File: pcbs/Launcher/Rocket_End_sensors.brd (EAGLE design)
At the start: 100 x 80 mm, 5 parts, among them U1 ARDUINO-MEGAPRO-5V, X1 22-23-2051, X3 22-23-2041

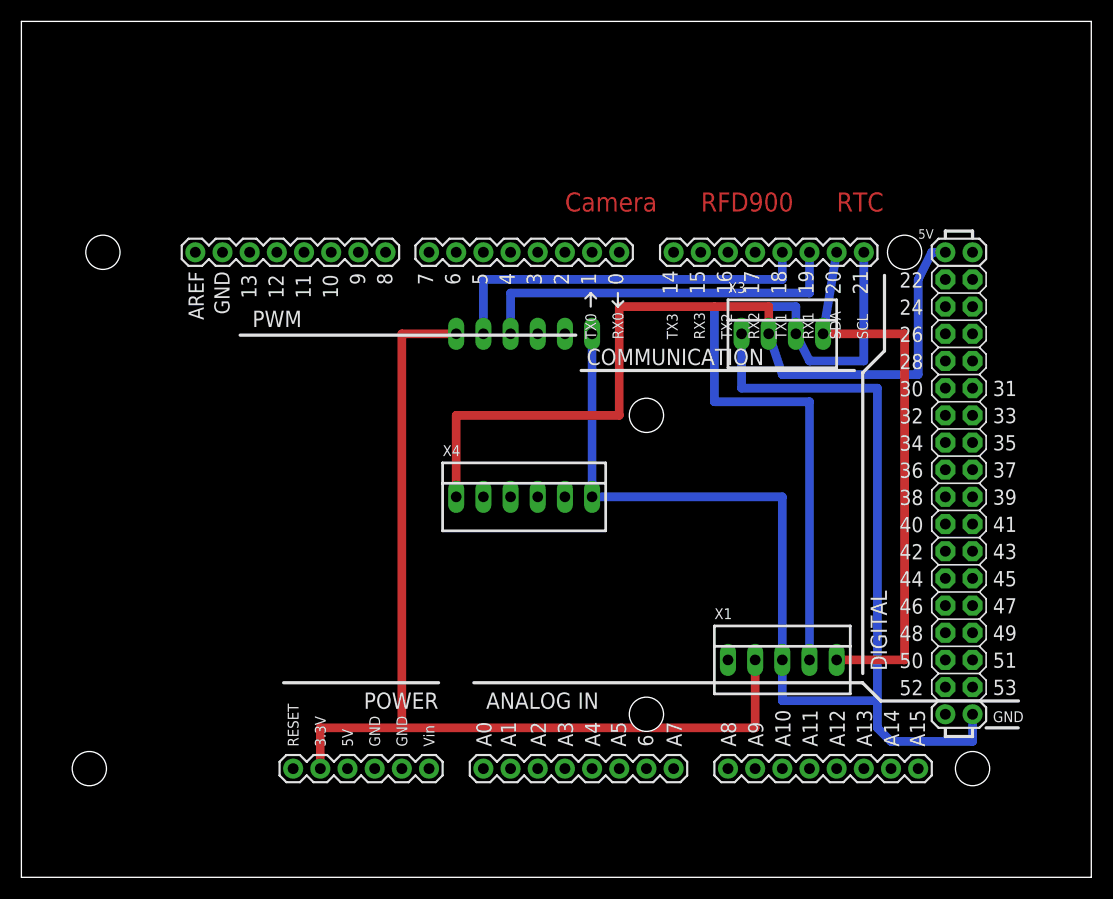
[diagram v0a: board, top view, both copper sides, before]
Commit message: * Adding GPS Module
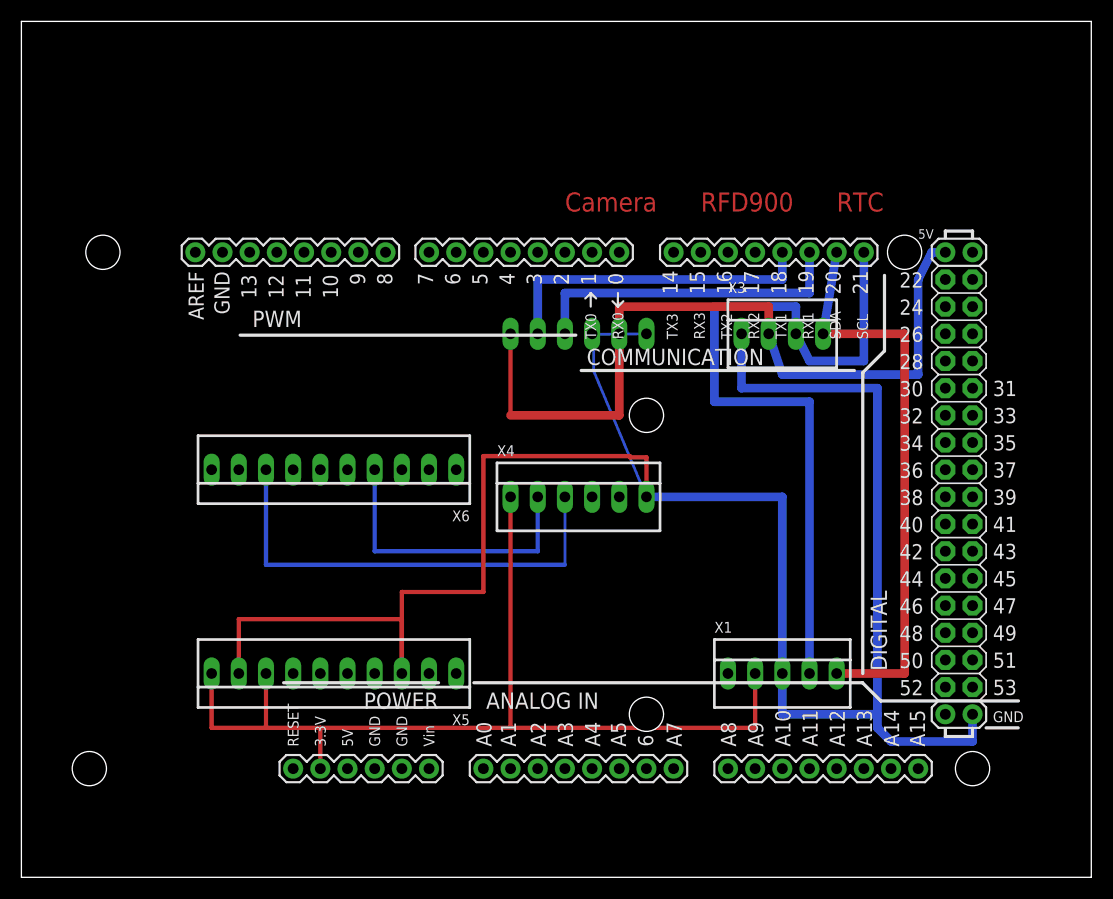
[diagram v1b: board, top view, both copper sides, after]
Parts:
- added X5, X6: 22-23-2101, con-molex:22-23-2101
- moved X2 5.08 mm to (52.1, 50.8)
- moved X4 5.08 mm to (52.1, 35.6)
- moved X1 1.27 mm to (71.1, 19.1)
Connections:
- removed net N$2: U1.3.3V, X1.2, X2.6
- removed net N$5: X4.3
- new net N$4: U1.3.3V, X1.2, X4.1, X5.10, X5.8
- new net N$8: X4.2, X6.4
- net GND: now also X5.3, X5.9
- net N$28: now also X2.6; no longer X4.1
- net N$6: now also X4.3, X6.8; no longer X4.2
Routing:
- net N$2: track 92.7 -> 0.00 mm
- net N$4: track 0.00 -> 91.4 mm
- net GND: track 122.4 -> 196.9 mm
- net N$6: track 0.00 -> 43.2 mm
- net N$8: track 0.00 -> 27.9 mm
- net N$3: track 35.6 -> 30.5 mm
- net N$28: track 79.2 -> 74.2 mm
- net N$1: track 35.6 -> 30.5 mm
- net N$24: track 70.1 -> 71.4 mm
- net N$18: track 52.2 -> 53.4 mm

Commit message: * Much better placement of components and tracks for Rocket_End * Put IMU on bottom of the Sensor board
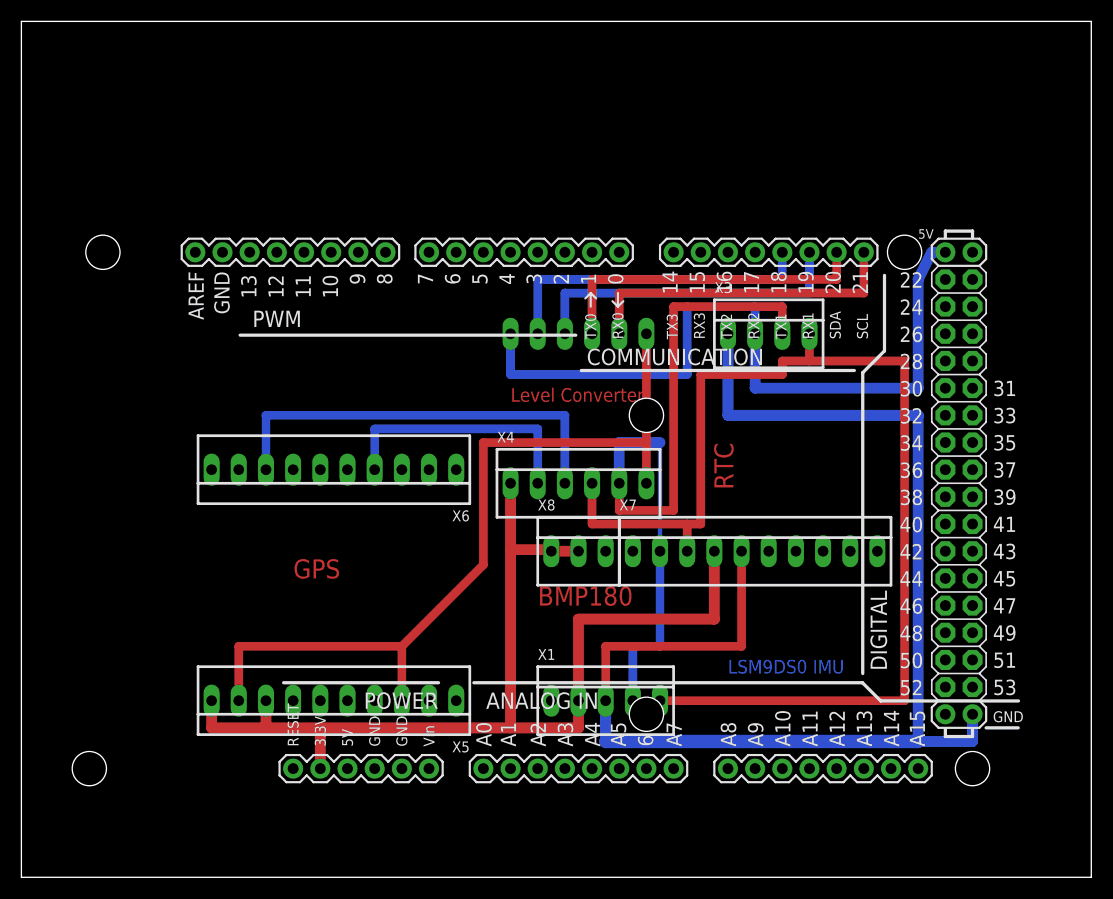
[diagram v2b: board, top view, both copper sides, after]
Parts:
- added X7: 22-23-2101, con-molex:22-23-2101
- added X8: 22-23-2031, con-molex:22-23-2031
- moved X1 16.7 mm to (54.6, 16.5)
- moved X5 2.54 mm to (29.2, 16.5)
- moved X3 1.27 mm to (69.8, 50.8)
- moved X4 1.27 mm to (52.1, 36.8)
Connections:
- new net N$2: U1.21, X2.2
- new net N$5: U1.20, X2.3
- new net N$7: X2.1, X4.6, X5.3, X5.9
- net GND: now also X7.5; no longer X2.1, X4.6, X5.3, X5.9
- net N$18: now also X4.4, X7.3; no longer U1.20
- net N$24: now also X4.5, X7.2; no longer U1.21
- net N$4: now also X7.4, X8.1, X8.2
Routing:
- net N$7: track 0.00 -> 76.8 mm
- net GND: track 196.9 -> 123.2 mm
- net N$18: track 53.4 -> 107.9 mm
- net N$5: track 0.00 -> 30.5 mm
- net N$2: track 0.00 -> 30.5 mm
- net N$4: track 91.4 -> 101.7 mm
- net N$28: track 74.2 -> 70.1 mm
- net N$8: track 27.9 -> 24.1 mm
- net N$6: track 43.2 -> 39.4 mm
- net N$24: track 71.4 -> 73.7 mm
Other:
- board text added: "BMP180"
- board text added: "GPS"
- board text added: "LSM9DS0 IMU"
- board text added: "Level Converter"
- board text removed: "Camera"
- board text removed: "RFD900"

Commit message: * using Via to ensure soldering is done on correct side.
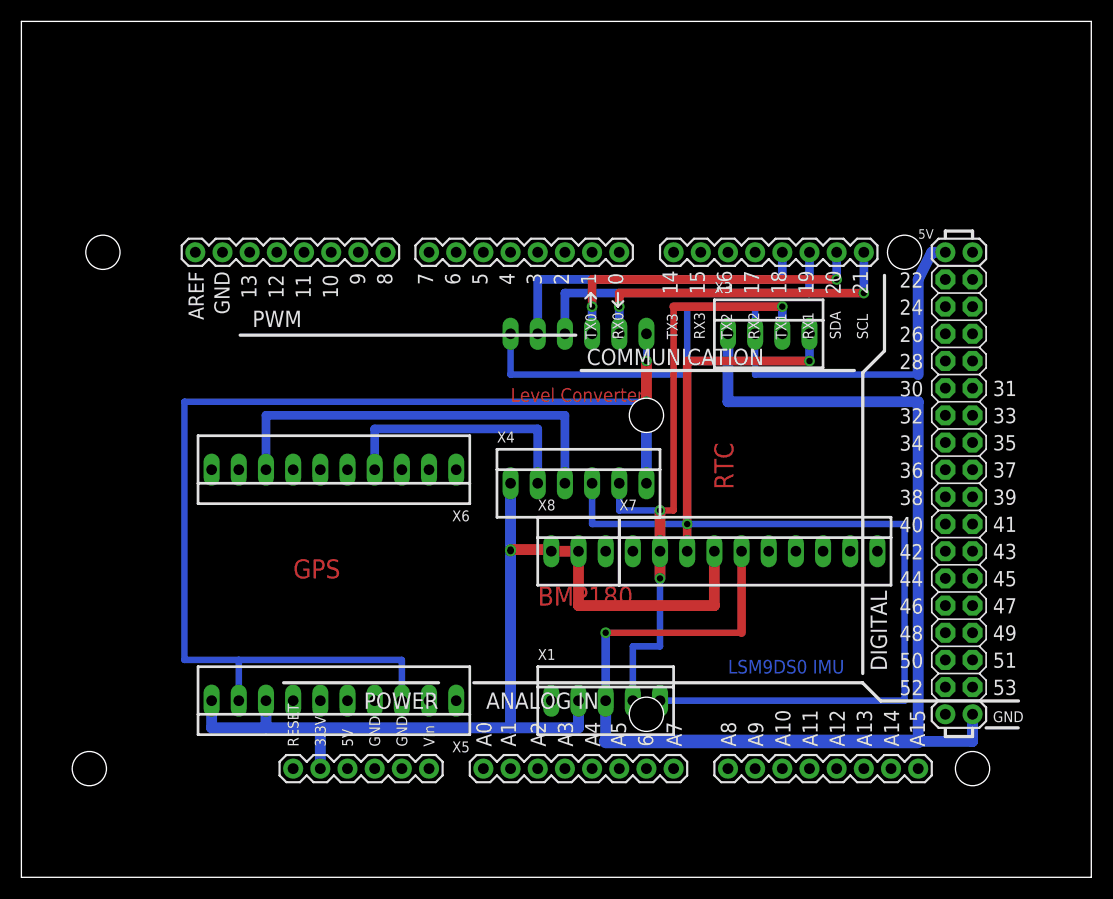
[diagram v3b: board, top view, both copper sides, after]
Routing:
- net N$7: track 76.8 -> 109.2 mm, vias 0 -> 2
- net N$24: track 73.7 -> 59.7 mm, vias 0 -> 3
- net N$4: track 101.7 -> 97.7 mm, vias 0 -> 2
- net N$18: track 107.9 -> 104.1 mm, vias 0 -> 2
- net N$28: track 70.1 -> 67.6 mm
- net N$5: vias 0 -> 2
- net N$2: vias 0 -> 2
- net GND: vias 0 -> 1

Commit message: * More mods....fixed up gps wiring. * Making place where can run some wires underneath so don't need   two sides for relay board.
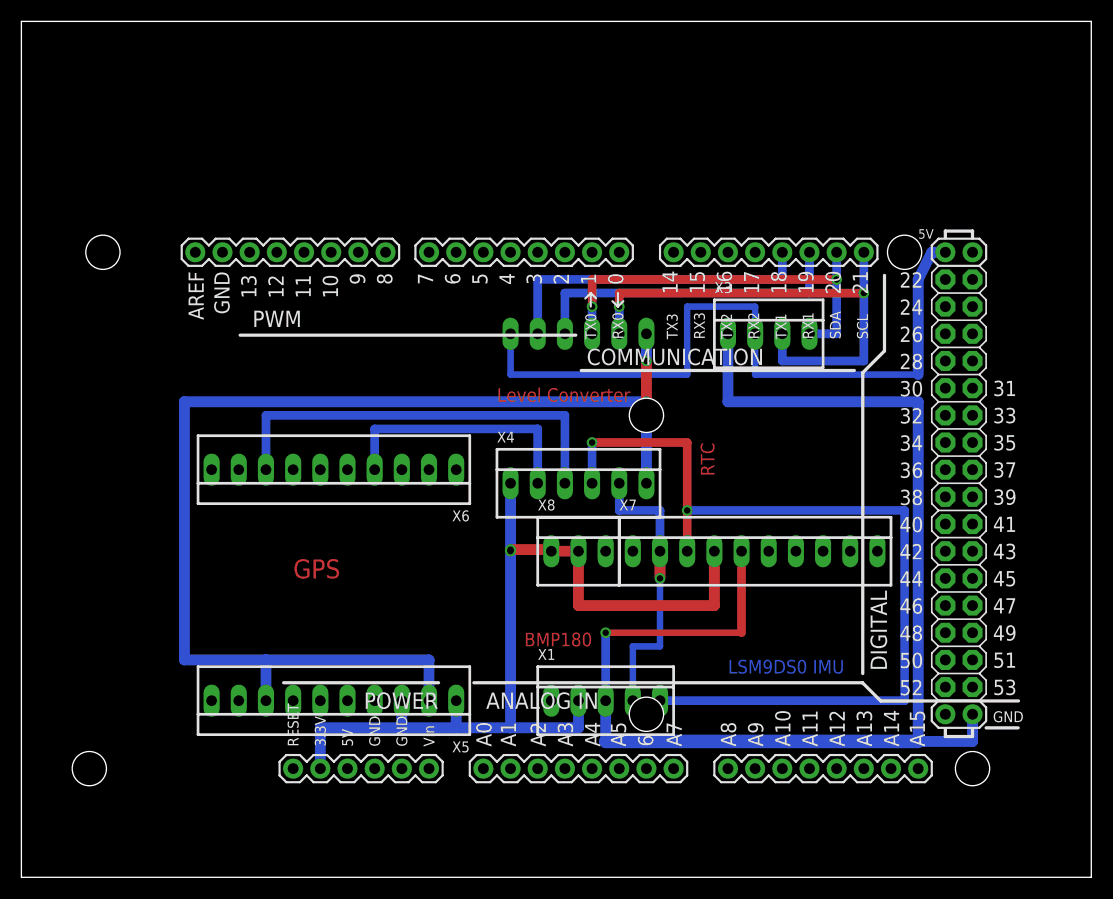
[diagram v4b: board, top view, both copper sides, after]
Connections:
- net N$18: no longer X3.4
- net N$2: now also X3.3
- net N$24: no longer X3.3
- net N$4: now also X5.1, X5.3; no longer X5.10, X5.8
- net N$5: now also X3.4
- net N$7: now also X5.2, X5.8; no longer X5.3, X5.9
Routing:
- net N$24: track 59.7 -> 26.7 mm, vias 3 -> 1
- net N$18: track 104.1 -> 83.8 mm
- net N$2: track 30.5 -> 47.0 mm
- net N$4: track 97.7 -> 87.5 mm
- net N$5: track 30.5 -> 38.1 mm
- net N$7: track 109.2 -> 111.8 mm

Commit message: * Just putting latest updates in
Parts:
- moved X5 5.08 mm to (29.2, 21.6)
- moved X6 5.08 mm to (29.2, 43.2)
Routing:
- net N$4: track 87.5 -> 97.7 mm
- net N$6: track 39.4 -> 38.4 mm
- net N$8: track 24.1 -> 23.4 mm
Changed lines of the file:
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@@
 <attribute name="MF" value="MOLEX" x="52.07" y="36.83" size="1.778" layer="27" display="off"/>
 </element>
-<element name="X6" library="con-molex" package="22-23-2101" value="22-23-2101" x="29.21" y="38.1" rot="R180">
-<attribute name="OC_NEWARK" value="94C0765" x="29.21" y="38.1" size="1.778" layer="27" rot="R180" display="off"/>
-<attribute name="MPN" value="22-23-2101" x="29.21" y="38.1" size="1.778" layer="27" rot="R180" display="off"/>
-<attribute name="MF" value="MOLEX" x="29.21" y="38.1" size="1.778" layer="27" rot="R180" display="off"/>
-<attribute name="OC_FARNELL" value="1756828" x="29.21" y="38.1" size="1.778" layer="27" rot="R180" display="off"/>
+<element name="X6" library="con-molex" package="22-23-2101" value="22-23-2101" x="29.21" y="43.18" rot="R180">
+<attribute name="OC_NEWARK" value="94C0765" x="29.21" y="43.18" size="1.778" layer="27" rot="R180" display="off"/>
+<attribute name="MPN" value="22-23-2101" x="29.21" y="43.18" size="1.778" layer="27" rot="R180" display="off"/>
+<attribute name="MF" value="MOLEX" x="29.21" y="43.18" size="1.778" layer="27" rot="R180" display="off"/>
+<attribute name="OC_FARNELL" value="1756828" x="29.21" y="43.18" size="1.778" layer="27" rot="R180" display="off"/>
 </element>
 <element name="X7" library="con-molex" package="22-23-2101" value="22-23-2101" x="68.58" y="30.48">
@@
 <attribute name="OC_FARNELL" value="1462950" x="52.07" y="30.48" size="1.778" layer="27" display="off"/>
 </element>
-<element name="X5" library="con-molex" package="22-23-2101" value="22-23-2101" x="29.21" y="16.51" rot="R180">
-<attribute name="OC_NEWARK" value="94C0765" x="29.21" y="16.51" size="1.778" layer="27" rot="R180" display="off"/>
-<attribute name="MPN" value="22-23-2101" x="29.21" y="16.51" size="1.778" layer="27" rot="R180" display="off"/>
-<attribute name="MF" value="MOLEX" x="29.21" y="16.51" size="1.778" layer="27" rot="R180" display="off"/>
-<attribute name="OC_FARNELL" value="1756828" x="29.21" y="16.51" size="1.778" layer="27" rot="R180" display="off"/>
+<element name="X5" library="con-molex" package="22-23-2101" value="22-23-2101" x="29.21" y="21.59" rot="R180">
+<attribute name="OC_NEWARK" value="94C0765" x="29.21" y="21.59" size="1.778" layer="27" rot="R180" display="off"/>
+<attribute name="MPN" value="22-23-2101" x="29.21" y="21.59" size="1.778" layer="27" rot="R180" display="off"/>
+<attribute name="MF" value="MOLEX" x="29.21" y="21.59" size="1.778" layer="27" rot="R180" display="off"/>
+<attribute name="OC_FARNELL" value="1756828" x="29.21" y="21.59" size="1.778" layer="27" rot="R180" display="off"/>
 </element>
 </elements>
@@
 <contactref element="X5" pad="1"/>
 <contactref element="X5" pad="3"/>
-<wire x1="40.64" y1="16.51" x2="40.64" y2="13.97" width="1.016" layer="16"/>
-<wire x1="35.56" y1="16.51" x2="35.56" y2="13.97" width="1.016" layer="16"/>
+<wire x1="40.64" y1="21.59" x2="40.64" y2="13.97" width="1.016" layer="16"/>
+<wire x1="35.56" y1="21.59" x2="35.56" y2="13.97" width="1.016" layer="16"/>
 <wire x1="45.72" y1="30.48" x2="45.72" y2="30.6324" width="0" layer="19" extent="16-16"/>
 </signal>
@@
 <contactref element="X6" pad="4"/>
 <contactref element="X4" pad="2"/>
-<wire x1="33.02" y1="38.1" x2="33.02" y2="41.91" width="0.8128" layer="16"/>
-<wire x1="33.02" y1="41.91" x2="48.26" y2="41.91" width="0.8128" layer="16"/>
-<wire x1="48.26" y1="41.91" x2="48.26" y2="36.83" width="0.8128" layer="16"/>
+<wire x1="33.02" y1="43.18" x2="33.02" y2="38.1" width="0.8128" layer="16"/>
+<wire x1="33.02" y1="38.1" x2="43.18" y2="38.1" width="0.8128" layer="16"/>
+<wire x1="43.18" y1="38.1" x2="44.45" y2="39.37" width="0.8128" layer="16"/>
+<wire x1="44.45" y1="39.37" x2="48.26" y2="39.37" width="0.8128" layer="16"/>
+<wire x1="48.26" y1="39.37" x2="48.26" y2="36.83" width="0.8128" layer="16"/>
 </signal>
 <signal name="N$6">
 <contactref element="X6" pad="8"/>
 <contactref element="X4" pad="3"/>
-<wire x1="22.86" y1="38.1" x2="22.86" y2="43.18" width="0.8128" layer="16"/>
-<wire x1="22.86" y1="43.18" x2="50.8" y2="43.18" width="0.8128" layer="16"/>
-<wire x1="50.8" y1="43.18" x2="50.8" y2="36.83" width="0.8128" layer="16"/>
+<wire x1="22.86" y1="43.18" x2="22.86" y2="45.72" width="0.8128" layer="16"/>
+<wire x1="22.86" y1="45.72" x2="43.18" y2="45.72" width="0.8128" layer="16"/>
+<wire x1="43.18" y1="45.72" x2="43.18" y2="44.45" width="0.8128" layer="16"/>
+<wire x1="43.18" y1="44.45" x2="44.45" y2="41.91" width="0.8128" layer="16"/>
+<wire x1="44.45" y1="41.91" x2="50.8" y2="41.91" width="0.8128" layer="16"/>
+<wire x1="50.8" y1="41.91" x2="50.8" y2="36.83" width="0.8128" layer="16"/>
 </signal>
 <signal name="N$2">
@@
 <contactref element="X2" pad="1"/>
 <wire x1="58.42" y1="50.8" x2="58.42" y2="48.26" width="1.016" layer="16"/>
-<wire x1="58.42" y1="48.26" x2="58.42" y2="44.45" width="1.016" layer="1"/>
-<wire x1="58.42" y1="44.45" x2="58.42" y2="36.83" width="1.016" layer="16"/>
-<via x="58.42" y="44.45" extent="1-16" drill="0.6" shape="square"/>
+<wire x1="58.42" y1="48.26" x2="58.42" y2="45.72" width="1.016" layer="1"/>
+<wire x1="58.42" y1="45.72" x2="58.42" y2="36.83" width="1.016" layer="16"/>
+<via x="58.42" y="45.72" extent="1-16" drill="0.6" shape="square"/>
 <via x="58.42" y="48.26" extent="1-16" drill="0.6" shape="square"/>
-<wire x1="22.86" y1="20.32" x2="38.1" y2="20.32" width="1.016" layer="16"/>
-<wire x1="22.86" y1="20.32" x2="15.24" y2="20.32" width="1.016" layer="16"/>
-<wire x1="15.24" y1="20.32" x2="15.24" y2="44.45" width="1.016" layer="16"/>
-<wire x1="15.24" y1="44.45" x2="58.42" y2="44.45" width="1.016" layer="16"/>
+<wire x1="22.86" y1="25.4" x2="38.1" y2="25.4" width="1.016" layer="16"/>
+<wire x1="22.86" y1="25.4" x2="15.24" y2="25.4" width="1.016" layer="16"/>
+<wire x1="15.24" y1="25.4" x2="15.24" y2="48.26" width="1.016" layer="16"/>
+<wire x1="15.24" y1="48.26" x2="43.18" y2="48.26" width="1.016" layer="16"/>
+<wire x1="43.18" y1="48.26" x2="45.72" y2="45.72" width="1.016" layer="16"/>
+<wire x1="45.72" y1="45.72" x2="58.42" y2="45.72" width="1.016" layer="16"/>
 <contactref element="X5" pad="2"/>
 <contactref element="X5" pad="8"/>
-<wire x1="38.1" y1="16.51" x2="38.1" y2="20.32" width="1.016" layer="16"/>
-<wire x1="22.86" y1="16.51" x2="22.86" y2="20.32" width="1.016" layer="16"/>
+<wire x1="38.1" y1="21.59" x2="38.1" y2="25.4" width="1.016" layer="16"/>
+<wire x1="22.86" y1="21.59" x2="22.86" y2="25.4" width="1.016" layer="16"/>
 </signal>
 </signals>
